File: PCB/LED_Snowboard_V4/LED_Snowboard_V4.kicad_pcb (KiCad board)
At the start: 4 copper layers, 100 x 100 mm, 114 parts, among them J1 Charge_Balance, J10 Output, J11 Micro_SD_Card_Det_Hirose_DM3AT, J12 Power Switch, J2 Bat2_Balance, J3 Bat1_Balance, J4 Bat1, J5 Bat2, J7 LED Data, J8 Sensor Input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

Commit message: trasnsfer
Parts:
- moved TP2 32.7 mm to (138.3, 100.4)
- moved R10 20.2 mm to (150.0, 100.4), turned to 180 degrees
- moved C1 16.6 mm to (151.5, 106.0), turned to 180 degrees
- moved U2 10.3 mm to (152.6, 109.0), turned to 180 degrees
- moved D2 9.28 mm to (153.0, 112.8)
- moved D1 8.62 mm to (155.1, 112.8)
- moved D13 8.51 mm to (163.6, 111.4), turned to 90 degrees
- moved C5 6.44 mm to (132.4, 106.0)
- moved C3 6.09 mm to (132.1, 111.7)
- moved D15 6.09 mm to (138.3, 115.2)
- moved F2 6.09 mm to (138.3, 112.7)
- moved L2 6.09 mm to (138.3, 108.7)
- moved U5 6.09 mm to (132.2, 108.7)
- moved Q4 6.09 mm to (145.3, 110.6)
- moved TP4 6.09 mm to (143.7, 119.6)
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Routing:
- net /IO and Power/DATA_1: track 5.38 -> 95.9 mm
- net /IO and Power/GATE_SIGNAL: track 2.81 -> 92.3 mm, vias 0 -> 1
- net /IO and Power/DATA_2: track 5.21 -> 87.2 mm
- net /IO and Power/DATA_3: track 7.00 -> 84.8 mm
- net /IO and Power/SW: track 11.6 -> 81.9 mm
- net /IO and Power/DT: track 7.00 -> 77.1 mm
- net /IO and Power/CLK: track 7.62 -> 76.6 mm
- net /IO and Power/SENSOR: track 8.45 -> 72.0 mm, vias 0 -> 1
- net VCC: track 9.37 -> 59.7 mm
- net /esp32/SD_SW: track 5.24 -> 53.4 mm, vias 0 -> 1
- net Net-(J12-Pin_2): track 0.00 -> 47.0 mm
- net /esp32/MOSI: track 5.99 -> 51.2 mm
- net /IO and Power/CELL1: track 4.06 -> 41.3 mm
- net /esp32/MISO: track 8.49 -> 40.8 mm
- net /IO and Power/CELL3: track 3.35 -> 32.3 mm
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- added copper zone on B.Cu, net +BATT
- added copper zone on F.Cu, net +BATT
- added copper zone on B.Cu, net Net-(D13-K)
- added copper zone on B.Cu, net Net-(Q1-D)
- added copper zone on B.Cu, net VCC

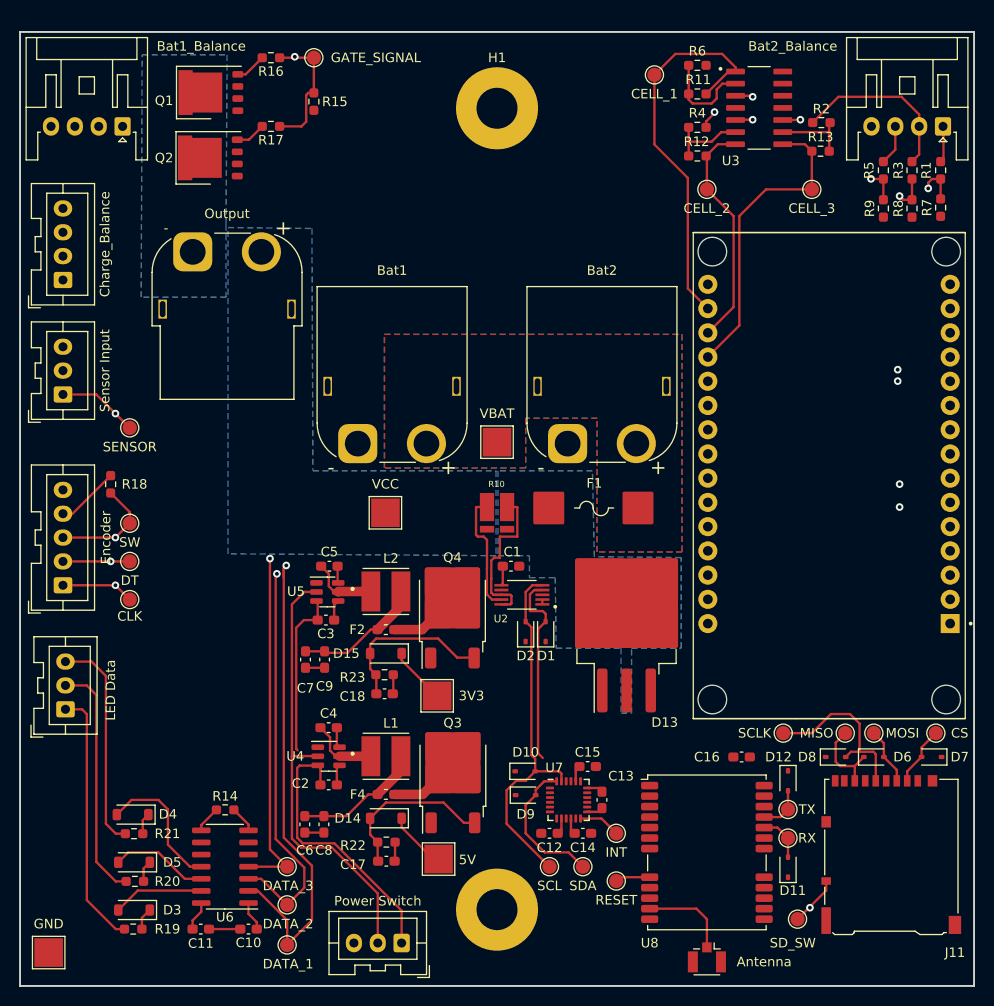
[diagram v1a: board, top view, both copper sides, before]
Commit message: routed all main lines and added power vias
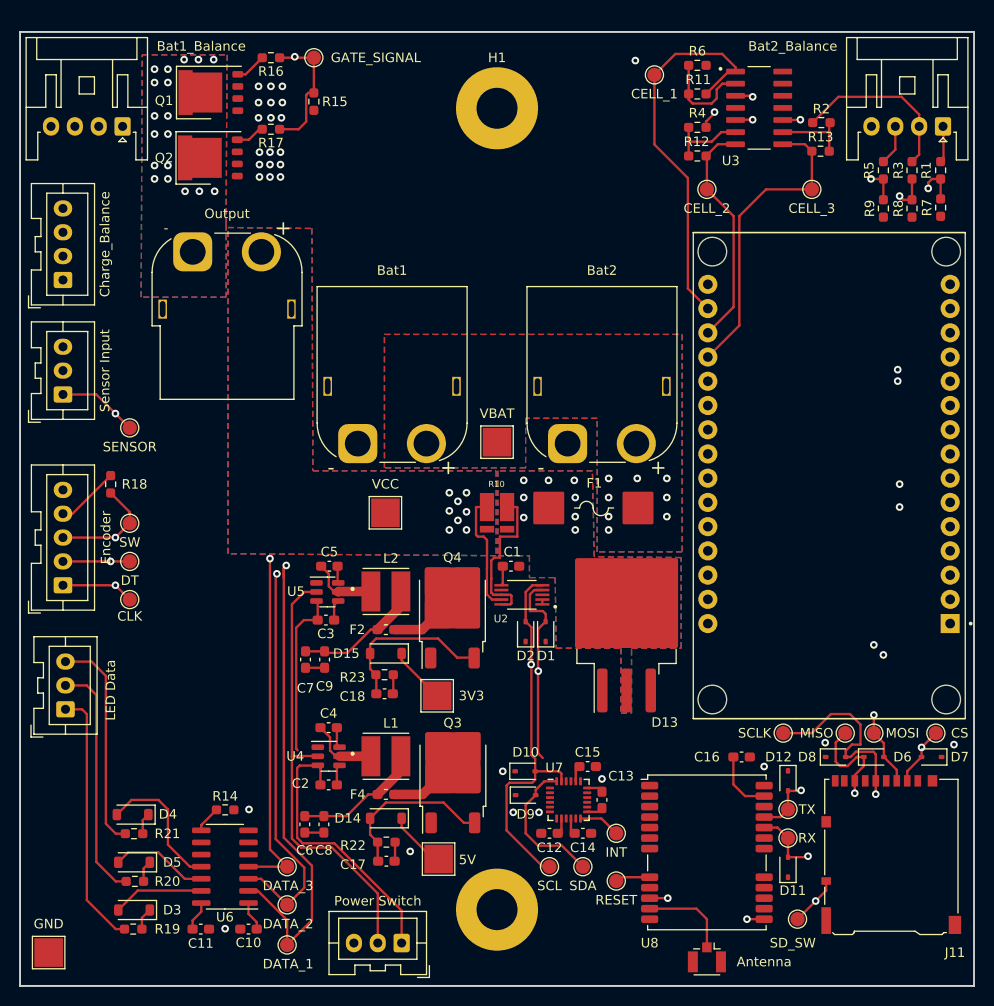
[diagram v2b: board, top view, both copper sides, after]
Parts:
- moved R17 0.30 mm to (126.3, 60.2)
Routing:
- net Net-(J1-Pin_1): track 3.83 -> 123.4 mm
- net Net-(J1-Pin_2): track 18.3 -> 136.6 mm
- net Net-(J1-Pin_3): track 29.3 -> 147.2 mm
- net /IO and Power/SCL: track 47.3 -> 117.0 mm, vias 1 -> 3
- net /IO and Power/SDA: track 41.2 -> 107.5 mm, vias 1 -> 3
- net /esp32/RX: track 10.5 -> 55.9 mm, vias 1 -> 2
- net /esp32/TX: track 10.3 -> 50.6 mm, vias 1 -> 2
- net /esp32/SCLK: track 45.7 -> 64.5 mm, vias 0 -> 1
- net /esp32/MISO: track 40.8 -> 56.7 mm, vias 0 -> 1
- net +3V3: track 26.5 -> 33.1 mm
- net /esp32/MOSI: track 51.2 -> 57.3 mm, vias 0 -> 1
- net /esp32/CS: track 32.9 -> 38.3 mm, vias 0 -> 1
- net /IO and Power/GATE_SIGNAL: track 92.3 -> 94.6 mm, vias 1 -> 2
- net GND: track 20.7 -> 18.5 mm, vias 0 -> 30
- net /esp32/SD_SW: track 53.4 -> 51.7 mm
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- added copper zone on F.Cu, net Net-(D13-K)
- added copper zone on F.Cu, net Net-(Q1-D)
- added copper zone on F.Cu, net VCC

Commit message: main routing complete v4
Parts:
- moved R15 14.0 mm to (144.0, 52.6), turned to 0 degrees
- moved TP9 0.40 mm to (127.6, 137.5)
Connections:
- C2 pad 2: VCC -> /IO and Power/GATE_SIGNAL
- C3 pad 2: VCC -> /IO and Power/GATE_SIGNAL
- J1 pad 1: Net-(J1-Pin_1) -> /IO and Power/GATE_SIGNAL
- J1 pad 2: Net-(J1-Pin_2) -> /IO and Power/GATE_SIGNAL
- J1 pad 3: Net-(J1-Pin_3) -> /IO and Power/GATE_SIGNAL
- J12 pad 1: VCC -> /IO and Power/GATE_SIGNAL
- J2 pad 1: Net-(J1-Pin_1) -> /IO and Power/GATE_SIGNAL
- J2 pad 2: Net-(J1-Pin_2) -> /IO and Power/GATE_SIGNAL
- J2 pad 3: Net-(J1-Pin_3) -> /IO and Power/GATE_SIGNAL
- J3 pad 1: Net-(J1-Pin_1) -> /IO and Power/GATE_SIGNAL
- J3 pad 2: Net-(J1-Pin_2) -> /IO and Power/GATE_SIGNAL
- J3 pad 3: Net-(J1-Pin_3) -> /IO and Power/GATE_SIGNAL
- J8 pad 1: /IO and Power/SENSOR -> /IO and Power/GATE_SIGNAL
- J9 pad 1: /IO and Power/CLK -> /IO and Power/GATE_SIGNAL
- J9 pad 2: /IO and Power/DT -> /IO and Power/GATE_SIGNAL
- J9 pad 3: /IO and Power/SW -> /IO and Power/GATE_SIGNAL
- R1 pad 1: Net-(J1-Pin_1) -> /IO and Power/GATE_SIGNAL
- R18 pad 2: /IO and Power/SW -> /IO and Power/GATE_SIGNAL
- R2 pad 1: Net-(J1-Pin_2) -> /IO and Power/GATE_SIGNAL
- R3 pad 2: Net-(J1-Pin_2) -> /IO and Power/GATE_SIGNAL
- R4 pad 1: Net-(J1-Pin_3) -> /IO and Power/GATE_SIGNAL
- R5 pad 1: Net-(J1-Pin_3) -> /IO and Power/GATE_SIGNAL
- TP19 pad 1: /IO and Power/SENSOR -> /IO and Power/GATE_SIGNAL
- TP22 pad 1: /IO and Power/SW -> /IO and Power/GATE_SIGNAL
- TP23 pad 1: /IO and Power/DT -> /IO and Power/GATE_SIGNAL
- TP24 pad 1: /IO and Power/CLK -> /IO and Power/GATE_SIGNAL
- U1 pad 5: /IO and Power/SENSOR -> /IO and Power/GATE_SIGNAL
- U1 pad 7: /IO and Power/SW -> /IO and Power/GATE_SIGNAL
- U1 pad 8: /IO and Power/DT -> /IO and Power/GATE_SIGNAL
- U1 pad 9: /IO and Power/CLK -> /IO and Power/GATE_SIGNAL
- U4 pad 3: VCC -> /IO and Power/GATE_SIGNAL
- U5 pad 3: VCC -> /IO and Power/GATE_SIGNAL
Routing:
- net /IO and Power/GATE_SIGNAL: track 94.6 -> 1023.0 mm, vias 2 -> 13
- net Net-(J1-Pin_3): track 147.2 -> 0.00 mm, vias 1 -> 0
- net Net-(J1-Pin_2): track 136.6 -> 0.00 mm
- net Net-(J1-Pin_1): track 123.4 -> 0.00 mm
- net /IO and Power/SW: track 81.9 -> 0.00 mm, vias 1 -> 0
- net /IO and Power/DT: track 77.1 -> 0.00 mm, vias 1 -> 0
- net /IO and Power/CLK: track 76.6 -> 0.00 mm, vias 1 -> 0
- net /IO and Power/SENSOR: track 72.0 -> 0.00 mm, vias 1 -> 0
- net /esp32/RESET: track 3.67 -> 70.3 mm, vias 0 -> 1
- net /esp32/INT: track 4.39 -> 68.3 mm, vias 0 -> 2
- net VCC: track 59.7 -> 12.9 mm
- net GND: track 18.5 -> 37.3 mm, vias 30 -> 49
- net +3V3: track 33.1 -> 44.2 mm, vias 0 -> 11
- net Net-(U4-FB): track 13.6 -> 23.9 mm, vias 0 -> 2
- net Net-(U5-FB): track 13.6 -> 23.9 mm, vias 0 -> 2
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- added copper zone on In1.Cu, net +3V3
- added copper zone on In1.Cu, net +5V
- added copper zone on B.Cu, net GND
- added copper zone on F.Cu, net GND
- added copper zone on In1.Cu, net GND
- added copper zone on In2.Cu, net GND

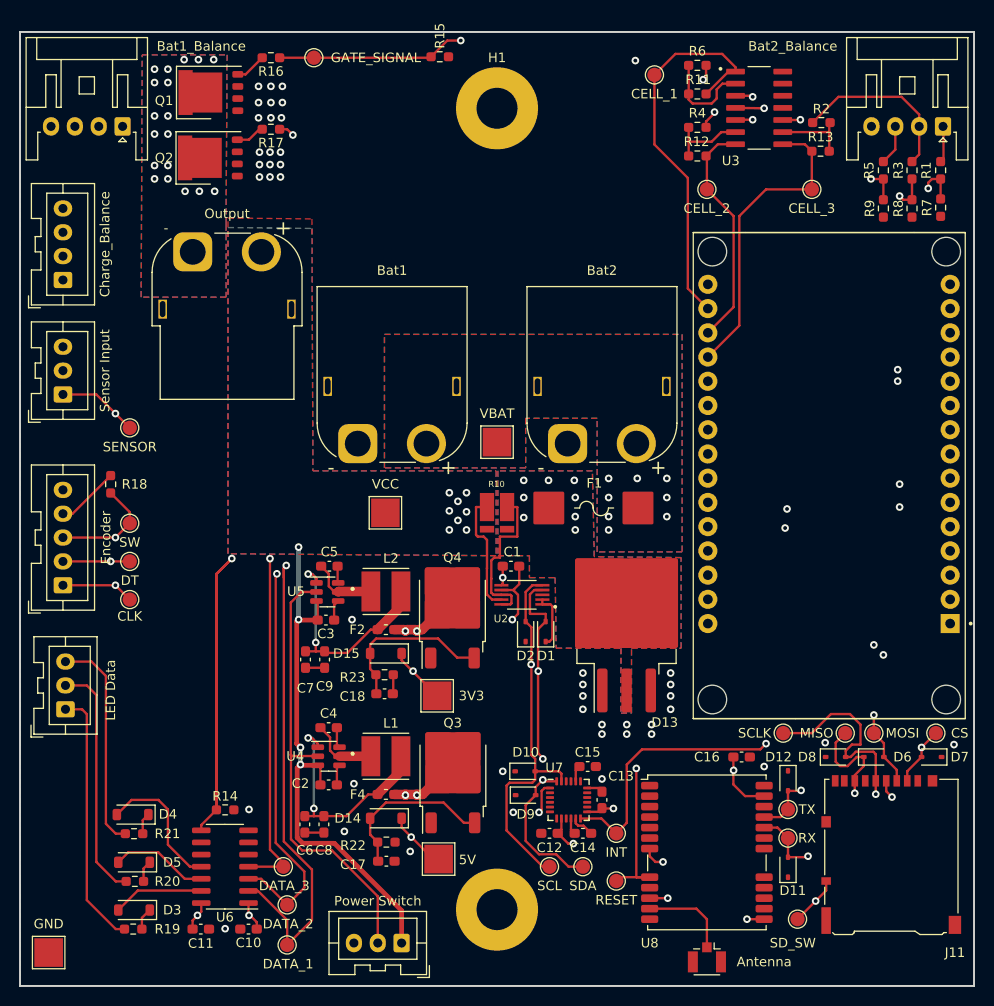
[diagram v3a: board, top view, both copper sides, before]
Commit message: Added all smd footprints
just need to add jst connectors and change gps antennae
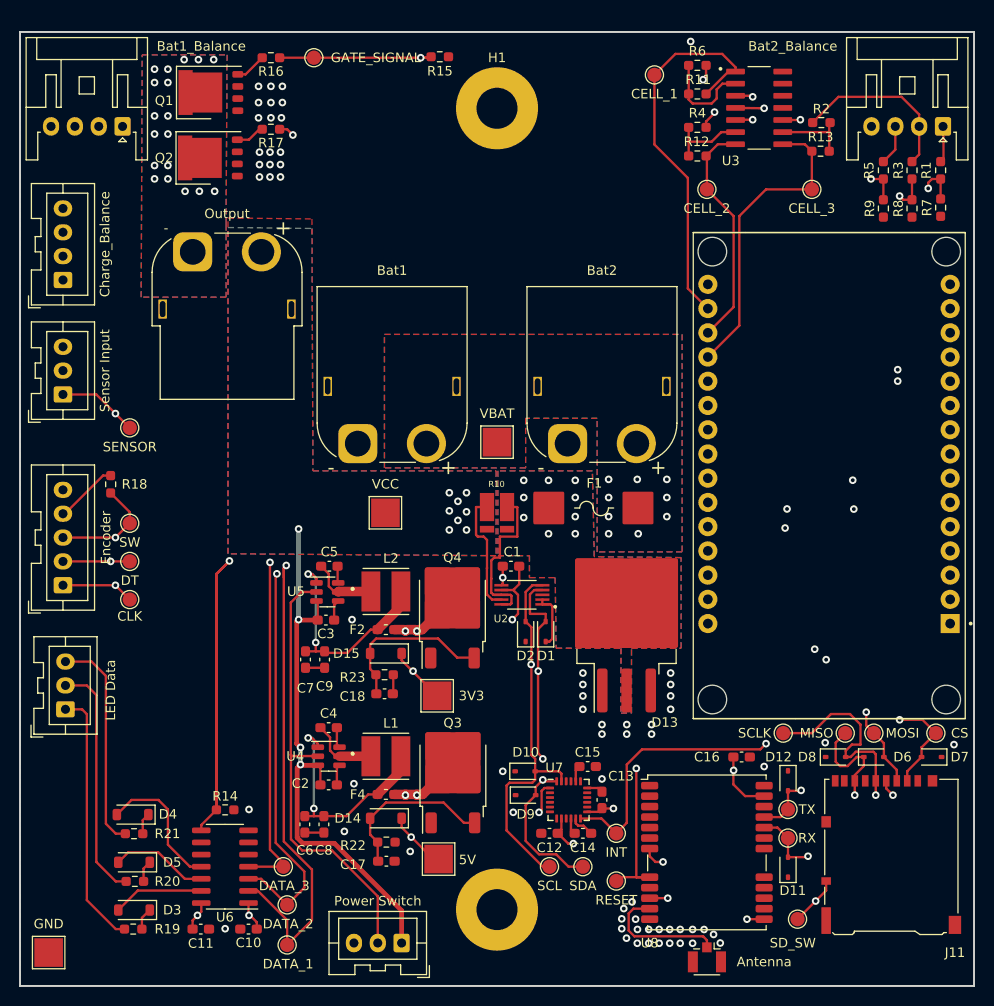
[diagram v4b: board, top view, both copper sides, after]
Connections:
- AE1 pad 2: (no net) -> GND
- C2 pad 2: /IO and Power/GATE_SIGNAL -> VCC
- C3 pad 2: /IO and Power/GATE_SIGNAL -> VCC
- J1 pad 1: /IO and Power/GATE_SIGNAL -> Net-(J1-Pin_1)
- J1 pad 2: /IO and Power/GATE_SIGNAL -> Net-(J1-Pin_2)
- J1 pad 3: /IO and Power/GATE_SIGNAL -> Net-(J1-Pin_3)
- J12 pad 1: /IO and Power/GATE_SIGNAL -> VCC
- J2 pad 1: /IO and Power/GATE_SIGNAL -> Net-(J1-Pin_1)
- J2 pad 2: /IO and Power/GATE_SIGNAL -> Net-(J1-Pin_2)
- J2 pad 3: /IO and Power/GATE_SIGNAL -> Net-(J1-Pin_3)
- J3 pad 1: /IO and Power/GATE_SIGNAL -> Net-(J1-Pin_1)
- J3 pad 2: /IO and Power/GATE_SIGNAL -> Net-(J1-Pin_2)
- J3 pad 3: /IO and Power/GATE_SIGNAL -> Net-(J1-Pin_3)
- J8 pad 1: /IO and Power/GATE_SIGNAL -> /IO and Power/SENSOR
- J9 pad 1: /IO and Power/GATE_SIGNAL -> /IO and Power/CLK
- J9 pad 2: /IO and Power/GATE_SIGNAL -> /IO and Power/DT
- J9 pad 3: /IO and Power/GATE_SIGNAL -> /IO and Power/SW
- R1 pad 1: /IO and Power/GATE_SIGNAL -> Net-(J1-Pin_1)
- R18 pad 2: /IO and Power/GATE_SIGNAL -> /IO and Power/SW
- R2 pad 1: /IO and Power/GATE_SIGNAL -> Net-(J1-Pin_2)
- R3 pad 2: /IO and Power/GATE_SIGNAL -> Net-(J1-Pin_2)
- R4 pad 1: /IO and Power/GATE_SIGNAL -> Net-(J1-Pin_3)
- R5 pad 1: /IO and Power/GATE_SIGNAL -> Net-(J1-Pin_3)
- TP19 pad 1: /IO and Power/GATE_SIGNAL -> /IO and Power/SENSOR
- TP22 pad 1: /IO and Power/GATE_SIGNAL -> /IO and Power/SW
- TP23 pad 1: /IO and Power/GATE_SIGNAL -> /IO and Power/DT
- TP24 pad 1: /IO and Power/GATE_SIGNAL -> /IO and Power/CLK
- U1 pad 5: /IO and Power/GATE_SIGNAL -> /IO and Power/SENSOR
- U1 pad 7: /IO and Power/GATE_SIGNAL -> /IO and Power/SW
- U1 pad 8: /IO and Power/GATE_SIGNAL -> /IO and Power/DT
- U1 pad 9: /IO and Power/GATE_SIGNAL -> /IO and Power/CLK
- U4 pad 3: /IO and Power/GATE_SIGNAL -> VCC
- U5 pad 3: /IO and Power/GATE_SIGNAL -> VCC
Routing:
- net /IO and Power/GATE_SIGNAL: track 1023.0 -> 226.3 mm, vias 13 -> 4
- net Net-(J1-Pin_3): track 0.00 -> 155.5 mm, vias 0 -> 1
- net Net-(J1-Pin_2): track 0.00 -> 146.1 mm
- net Net-(J1-Pin_1): track 0.00 -> 132.5 mm
- net /IO and Power/SW: track 0.00 -> 83.3 mm, vias 0 -> 1
- net /IO and Power/DT: track 0.00 -> 77.6 mm, vias 0 -> 1
- net /IO and Power/CLK: track 0.00 -> 76.8 mm, vias 0 -> 1
- net /IO and Power/SENSOR: track 0.00 -> 72.0 mm, vias 0 -> 1
- net VCC: track 12.9 -> 71.2 mm, vias 8 -> 12
- net Net-(AE1-A): track 9.41 -> 13.6 mm
- net /IO and Power/SDA: track 111.0 -> 107.6 mm
- net /IO and Power/SCL: track 117.0 -> 113.9 mm
- net /esp32/CS: track 38.3 -> 40.7 mm
- net /esp32/SCLK: track 64.5 -> 63.3 mm
- net /IO and Power/DATA_3: track 84.8 -> 84.1 mm
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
